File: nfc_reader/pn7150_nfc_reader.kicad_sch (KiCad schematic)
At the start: 26 parts, among them Y2 27.12MHz

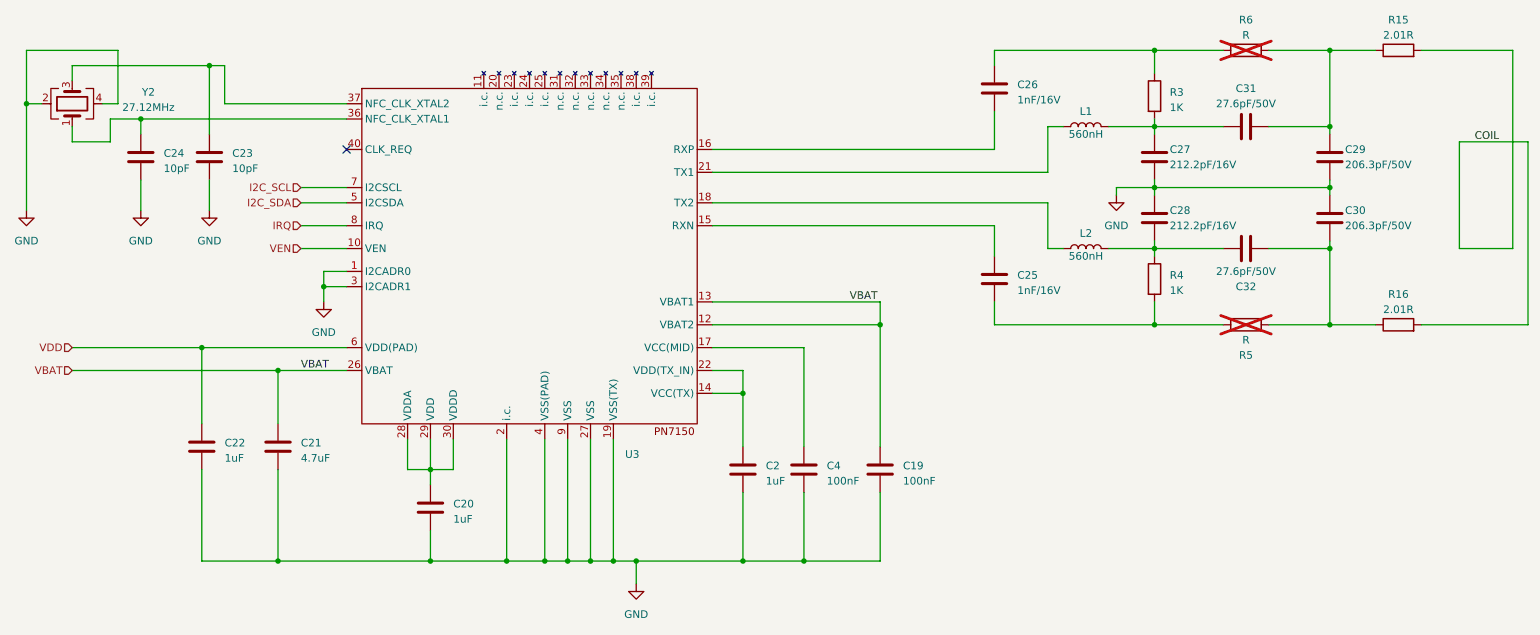
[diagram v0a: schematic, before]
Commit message: Added front artwork to nfc_reader
Also
- Fixed error with missing power to PN7150 radio
- Added two buttons and two LEDs
- Moved things around a little
- Updated BOM and created pos file
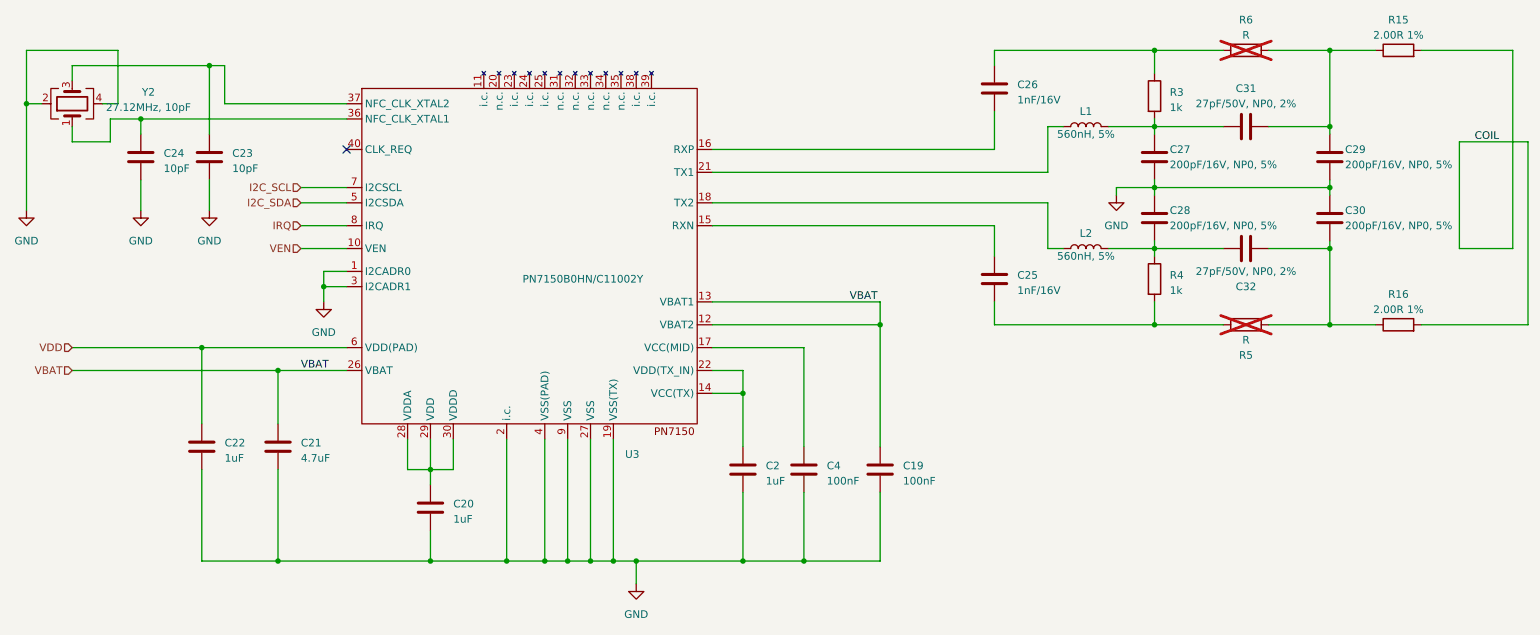
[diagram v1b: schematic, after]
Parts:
- C27, C28: value 212.2pF/16V -> 200pF/16V, NP0, 5%
- C29, C30: value 206.3pF/50V -> 200pF/16V, NP0, 5%
- C31, C32: value 27.6pF/50V -> 27pF/50V, NP0, 2%
- L1, L2: value 560nH -> 560nH, 5%
- R15, R16: value 2.01R -> 2.00R 1%
- R3, R4: value 1K -> 1k
- R5, R6: now left out of the parts list
- U3: value ~ -> PN7150B0HN/C11002Y
- Y2: value 27.12MHz -> 27.12MHz, 10pF
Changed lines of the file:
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@@
   (title_block
     (title "PN7150 NFC Reader")
-    (date "2023-05-07")
-    (rev "1.0")
+    (date "2023-06-22")
+    (rev "1.1")
     (comment 1 "CC-BY-SA")
   )
@@
       (effects (font (size 1.27 1.27)) (justify left))
     )
-    (property "Value" "1K" (at 217.17 88.265 0)
+    (property "Value" "1k" (at 217.17 88.265 0)
       (effects (font (size 1.27 1.27)) (justify left))
     )
@@
       (effects (font (size 1.27 1.27)) (justify left))
     )
-    (property "Value" "~" (at 119.38 86.36 0)
+    (property "Value" "PN7150B0HN/C11002Y" (at 119.38 86.36 0)
       (effects (font (size 1.27 1.27)))
     )
@@
       (effects (font (size 1.27 1.27)))
     )
-    (property "Value" "560nH" (at 203.2 62.23 90)
+    (property "Value" "560nH, 5%" (at 203.2 62.23 90)
       (effects (font (size 1.27 1.27)))
     )
@@
       (effects (font (size 1.27 1.27)))
     )
-    (property "Value" "27.12MHz" (at 46.99 57.7597 90)
+    (property "Value" "27.12MHz, 10pF" (at 46.99 57.7597 90)
       (effects (font (size 1.27 1.27)))
     )
@@
       (effects (font (size 1.27 1.27)))
     )
-    (property "Value" "2.01R" (at 255.27 45.72 90)
+    (property "Value" "2.00R 1%" (at 255.27 45.72 90)
       (effects (font (size 1.27 1.27)))
     )
@@
       (effects (font (size 1.27 1.27)) (justify left))
     )
-    (property "Value" "1K" (at 217.17 57.785 0)
+    (property "Value" "1k" (at 217.17 57.785 0)
       (effects (font (size 1.27 1.27)) (justify left))
     )
@@
       (effects (font (size 1.27 1.27)))
     )
-    (property "Value" "560nH" (at 203.2 82.55 90)
+    (property "Value" "560nH, 5%" (at 203.2 82.55 90)
       (effects (font (size 1.27 1.27)))
     )
@@
       (effects (font (size 1.27 1.27)))
     )
-    (property "Value" "27.6pF/50V" (at 229.87 57.15 90)
+    (property "Value" "27pF/50V, NP0, 2%" (at 229.87 57.15 90)
       (effects (font (size 1.27 1.27)))
     )
@@
   )
   (symbol (lib_id "Device:R") (at 229.87 48.26 90) (unit 1)
-    (in_bom yes) (on_board yes) (dnp yes) (fields_autoplaced)
+    (in_bom no) (on_board yes) (dnp yes) (fields_autoplaced)
     (property "Reference" "R6" (at 229.87 43.18 90)
       (effects (font (size 1.27 1.27)))
@@
   )
   (symbol (lib_id "Device:R") (at 229.87 93.98 90) (unit 1)
-    (in_bom yes) (on_board yes) (dnp yes)
+    (in_bom no) (on_board yes) (dnp yes)
     (property "Reference" "R5" (at 229.87 99.06 90)
       (effects (font (size 1.27 1.27)))
@@
       (effects (font (size 1.27 1.27)) (justify left))
     )
-    (property "Value" "212.2pF/16V" (at 217.17 77.47 0)
+    (property "Value" "200pF/16V, NP0, 5%" (at 217.17 77.47 0)
       (effects (font (size 1.27 1.27)) (justify left))
     )
@@
       (effects (font (size 1.27 1.27)) (justify left))
     )
-    (property "Value" "212.2pF/16V" (at 217.17 67.31 0)
+    (property "Value" "200pF/16V, NP0, 5%" (at 217.17 67.31 0)
       (effects (font (size 1.27 1.27)) (justify left))
     )
@@
       (effects (font (size 1.27 1.27)))
     )
-    (property "Value" "27.6pF/50V" (at 229.87 85.09 90)
+    (property "Value" "27pF/50V, NP0, 2%" (at 229.87 85.09 90)
       (effects (font (size 1.27 1.27)))
     )
@@
       (effects (font (size 1.27 1.27)))
     )
-    (property "Value" "2.01R" (at 255.27 91.44 90)
+    (property "Value" "2.00R 1%" (at 255.27 91.44 90)
       (effects (font (size 1.27 1.27)))
     )
@@
       (effects (font (size 1.27 1.27)) (justify left))
     )
-    (property "Value" "206.3pF/50V" (at 246.38 77.47 0)
+    (property "Value" "200pF/16V, NP0, 5%" (at 246.38 77.47 0)
       (effects (font (size 1.27 1.27)) (justify left))
     )
@@
       (effects (font (size 1.27 1.27)) (justify left))
     )
-    (property "Value" "206.3pF/50V" (at 246.38 67.31 0)
-      (effects (font (size 1.27 1.27)) (justify left))
-    )
+    (property "Value" "200pF/16V, NP0, 5%" (at 246.38 67.31 0)
+      (effects (font (size 1.27 1.27)) (justify left))
+    )
